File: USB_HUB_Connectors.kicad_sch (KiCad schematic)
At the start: 87 parts, among them IC4 AP22652W6-7, J10 E8124-015-01, J11 E8124-015-01, U15 USB57442G, Y2 ABM8G-25.000MHZ-B4Y-T

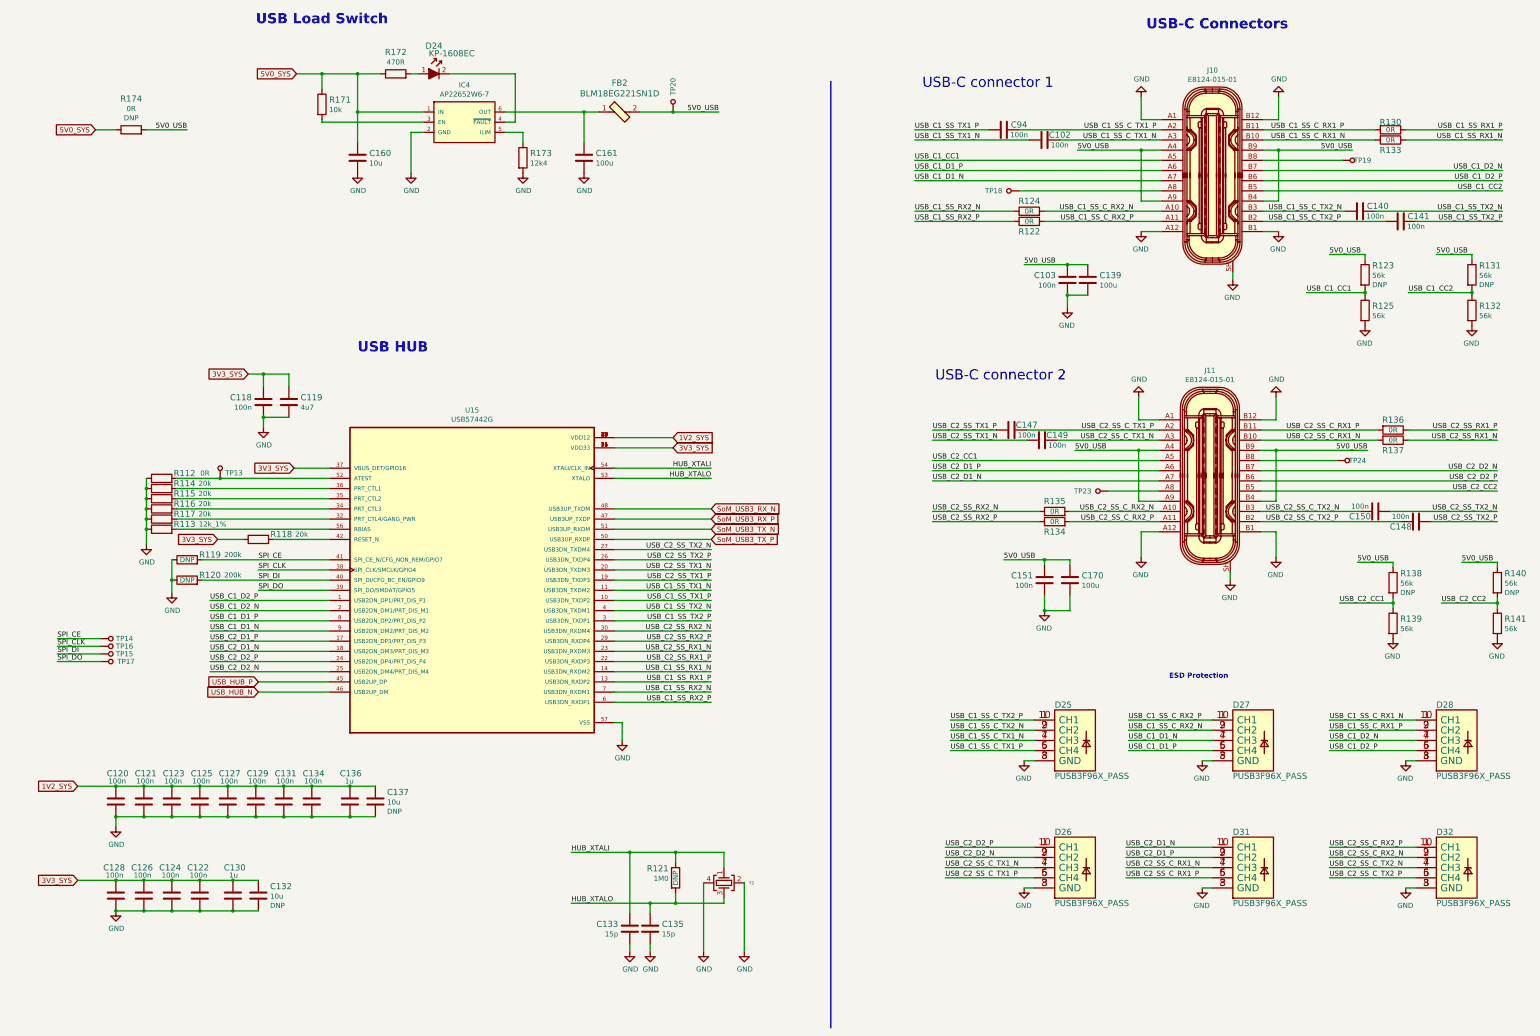
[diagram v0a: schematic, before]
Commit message: Introduce component standardization
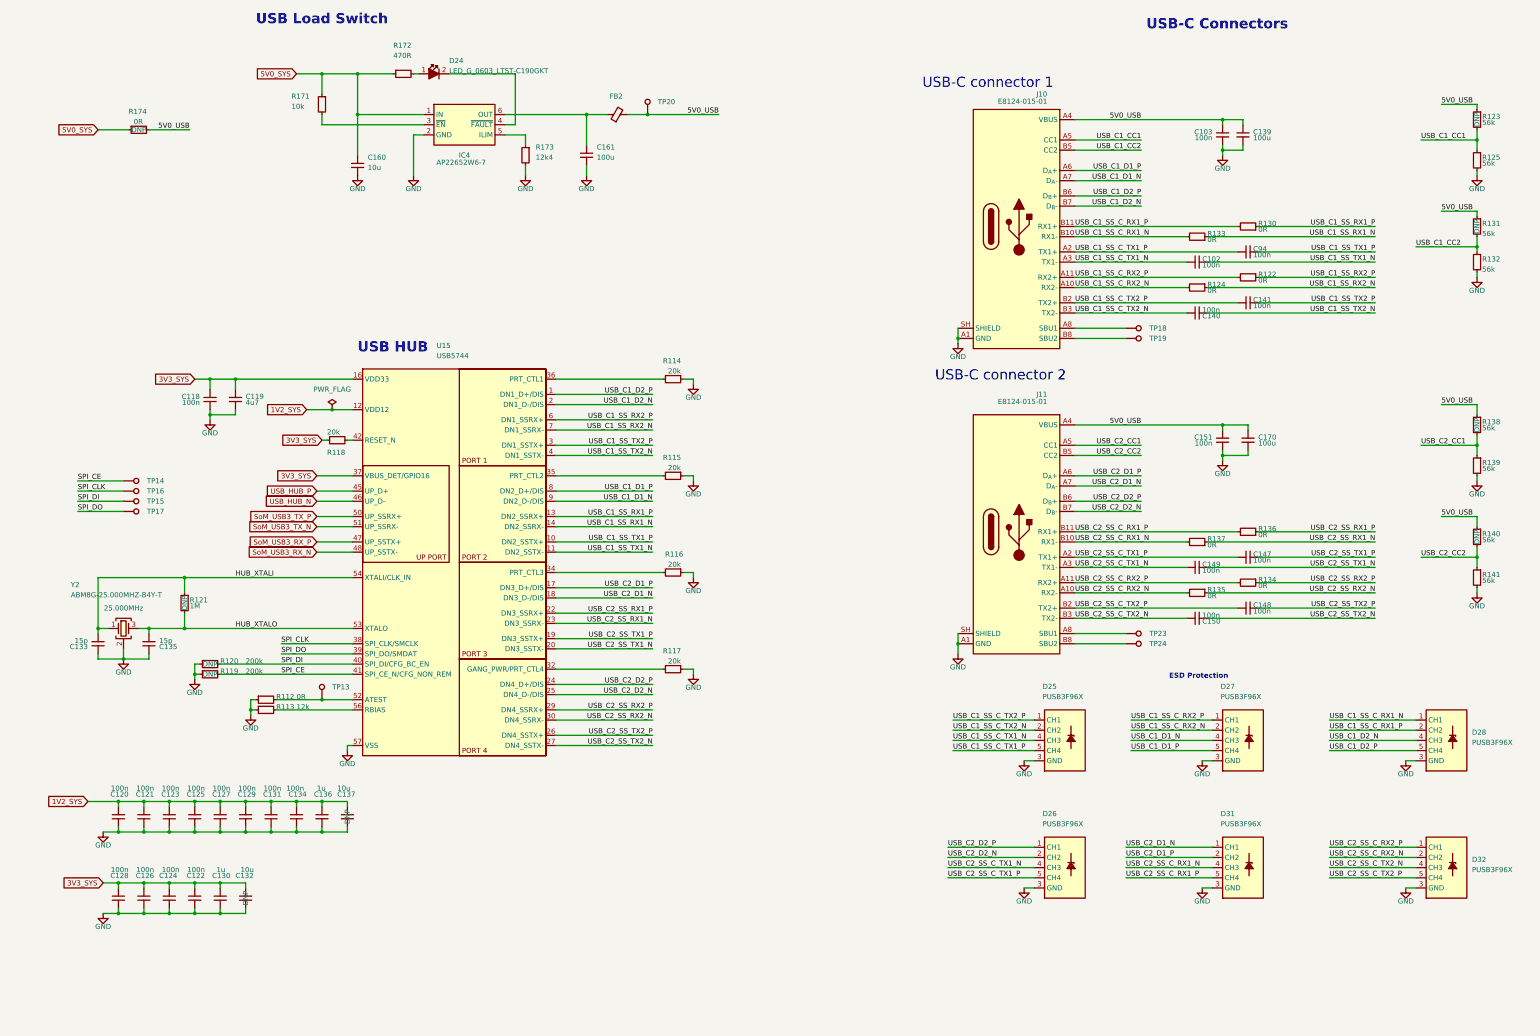
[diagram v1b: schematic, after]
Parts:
- C102, C103, C118, C120, C121, C122, C123, C124, C125, C126, C127, C128, C129, C131, C134, C140, C141, C147, C148, C149, C150, C151, C94: footprint sc606-baseboard-footprints:0402-cap -> sc606-baseboard-footprints:C_0402_1005Metric; Author (none) -> Antmicro; Dielectric (none) -> X5R; License (none) -> Apache-2.0; Voltage (none) -> 50V
- C119: footprint sc606-baseboard-footprints:0402-cap -> sc606-baseboard-footprints:C_0402_1005Metric; Author (none) -> Antmicro; License (none) -> Apache-2.0; Manufacturer MURATA -> Murata
- C130, C136: footprint sc606-baseboard-footprints:0402-cap -> sc606-baseboard-footprints:C_0402_1005Metric; Author (none) -> Antmicro; License (none) -> Apache-2.0
- C132, C137, C160: footprint sc606-baseboard-footprints:0402-cap -> sc606-baseboard-footprints:C_0402_1005Metric; Author (none) -> Antmicro; License (none) -> Apache-2.0; Manufacturer YAGEO -> Yaego
- C133, C135: footprint sc606-baseboard-footprints:0402-cap -> sc606-baseboard-footprints:C_0402_1005Metric; Author (none) -> Antmicro; License (none) -> Apache-2.0; Manufacturer MULTICOMP -> Multicomp
- C139, C161, C170: footprint sc606-baseboard-footprints:0805-cap -> sc606-baseboard-footprints:C_0805_2012Metric; Author (none) -> Antmicro; License (none) -> Apache-2.0; Manufacturer MURATA -> Murata
- D24: value KP-1608EC -> LED_G_0603_LTST-C190GKT; footprint sc606-baseboard-footprints:LED_0603 -> sc606-baseboard-footprints:LED_0603_1608Metric_G; symbol sc606-baseboard:KP-1608EC -> sc606-baseboard:LED_G_0603_LTST-C190GKT; Author (none) -> Antmicro; License (none) -> Apache-2.0; MPN KP-1608EC -> LTST-C190GKT; Manufacturer KINGBRIGHT -> Lite-On Inc.
- D25, D26, D27, D28, D31, D32: footprint sc606-baseboard-footprints:PUSB3F96X -> sc606-baseboard-footprints:Nexperia_DFN-10_2.5x1mm_P0.5mm; Author (none) -> Antmicro; License (none) -> Apache-2.0
- FB2: value BLM18EG221SN1D -> FB_220Z_1A_0603; footprint sc606-baseboard-footprints:0603 -> sc606-baseboard-footprints:FB_0603_1608Metric; symbol sc606-baseboard:BLM18EG221SN1D -> sc606-baseboard:FB_220Z_1A_0603; Author (none) -> Antmicro; License (none) -> Apache-2.0
- IC4: value AP22652W6-7 -> AP22652W6; symbol sc606-baseboard:AP22652W6-7 -> sc606-baseboard:AP22652W6; Author (none) -> Antmicro; License (none) -> Apache-2.0; Manufacturer Diodes Incorporated -> Diodes Incorporated
- J10, J11: value E8124-015-01 -> E8124-015-01_separate; symbol sc606-baseboard:E8124-015-01 -> sc606-baseboard:E8124-015-01_separate; Author (none) -> Antmicro; License (none) -> Apache-2.0; Manufacturer Pulse Electronics Network -> Pulse
- R112, R122, R124, R130, R133, R134, R135, R136, R137, R174: footprint sc606-baseboard-footprints:0402-res -> sc606-baseboard-footprints:R_0402_1005Metric; Author (none) -> Antmicro; Current (none) -> 1A; License (none) -> Apache-2.0; Manufacturer PANASONIC -> Panasonic
- R113: value R_12k_1%_0603 -> R_12k_0603; footprint sc606-baseboard-footprints:0603-res -> sc606-baseboard-footprints:R_0603_1608Metric; symbol sc606-baseboard:R_12k_1%_0603 -> sc606-baseboard:R_12k_0603; Author (none) -> Antmicro; License (none) -> Apache-2.0; MPN MCWR06X1202FTL -> CR0603-FX-1202ELF; Manufacturer MULTICOMP PRO -> Bourns; Tolerance (none) -> 1%; Val 12k_1% -> 12k
- R114, R115, R116, R117, R118: footprint sc606-baseboard-footprints:0402-res -> sc606-baseboard-footprints:R_0402_1005Metric; Author (none) -> Antmicro; License (none) -> Apache-2.0; MPN CRCW040220K0FKED -> CR0402-FX-2002GLF; Manufacturer VISHAY -> Bourns; Tolerance (none) -> 1%
- R119, R120: footprint sc606-baseboard-footprints:0402-res -> sc606-baseboard-footprints:R_0402_1005Metric; Author (none) -> Antmicro; License (none) -> Apache-2.0; MPN RC0402FR-07200KL -> CR0402-FX-2003GLF; Manufacturer YAGEO_(PHYCOMP) -> Bourns; Tolerance (none) -> 1%
- R121: value R_1M0_0402 -> R_1M_0402; footprint sc606-baseboard-footprints:0402-res -> sc606-baseboard-footprints:R_0402_1005Metric; symbol sc606-baseboard:R_1M0_0402 -> sc606-baseboard:R_1M_0402; Author (none) -> Antmicro; License (none) -> Apache-2.0; MPN CRG0402F1M0 -> CR0402-FX-1004GLF; Manufacturer TE CONNECTIVITY -> Bourns; Tolerance (none) -> 1%; Val 1M0 -> 1M
- R123, R125, R131, R132, R138, R139, R140, R141: footprint sc606-baseboard-footprints:0402-res -> sc606-baseboard-footprints:R_0402_1005Metric; Author (none) -> Antmicro; License (none) -> Apache-2.0; MPN CRCW040256K0FKED -> CR0402-FX-5602GLF; Manufacturer VISHAY -> Bourns; Tolerance (none) -> 1%
- R171: footprint sc606-baseboard-footprints:0402-res -> sc606-baseboard-footprints:R_0402_1005Metric; Author (none) -> Antmicro; License (none) -> Apache-2.0; MPN CRCW040210K0FKEDHP -> CR0402-FX-1002GLF; Manufacturer VISHAY -> Bourns; Tolerance (none) -> 1%
- R172: footprint sc606-baseboard-footprints:0402-res -> sc606-baseboard-footprints:R_0402_1005Metric; Author (none) -> Antmicro; License (none) -> Apache-2.0; MPN CRCW0402470RFKED -> CR0402-FX-4700GLF; Manufacturer VISHAY -> Bourns; Tolerance (none) -> 1%
- R173: footprint sc606-baseboard-footprints:0402-res -> sc606-baseboard-footprints:R_0402_1005Metric; Author (none) -> Antmicro; License (none) -> Apache-2.0; MPN ERJ2RKF1242X -> CR0402-FX-1242GLF; Manufacturer PANASONIC_ELECTRONIC_COMPONENTS -> Bourns; Tolerance (none) -> 1%
- TP13, TP14, TP15, TP16, TP17: value TP_SMD_1_5MM -> TP_1.5mm_SMD; footprint sc606-baseboard-footprints:TP-R-1.5 -> sc606-baseboard-footprints:TP_SMD_1.5mm; symbol sc606-baseboard:TP_SMD_0_75MM-antmicroTestPoints -> sc606-baseboard:TP_1.5mm_SMD; Author (none) -> Antmicro; License (none) -> Apache-2.0
- TP18, TP19, TP20, TP23, TP24: value TP_SMD_1_5MM -> TP_1.5mm_SMD; footprint sc606-baseboard-footprints:TP-R-1.5 -> sc606-baseboard-footprints:TP_SMD_1.5mm; symbol sc606-baseboard:TP_SMD_0_75MM -> sc606-baseboard:TP_1.5mm_SMD; Author (none) -> Antmicro; License (none) -> Apache-2.0
- U15: footprint sc606-baseboard-footprints:QFN40P700X700X100-57N -> sc606-baseboard-footprints:QFN-56-1EP_7x7mm_P0.4mm_EP4.6x4.6mm; Author (none) -> Antmicro; License (none) -> Apache-2.0; Manufacturer MICROCHIP -> Microchip
- Y2: footprint sc606-baseboard-footprints:KX-7 -> sc606-baseboard-footprints:Oscillator_SMD_Geyer_KX-7-4Pin_3.2x2.5mm; Author (none) -> Antmicro; License (none) -> Apache-2.0; Val (none) -> 25.000MHz
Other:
- moved on the sheet: C102, C103, C118, C119, C120, C121, C122, C123, C124, C125, C126, C127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

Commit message: [#61796] Run globlib
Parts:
- C102, C103, C118, C120, C121, C122, C123, C124, C125, C126, C127, C128, C129, C131, C134, C140, C141, C147, C148, C149, C150, C151, C94: footprint sc606-baseboard-footprints:C_0402_1005Metric -> antmicro-footprints:C_0402_1005Metric; symbol sc606-baseboard:C_100n_0402 -> antmicroCapacitors0402:C_100n_0402
- C119: footprint sc606-baseboard-footprints:C_0402_1005Metric -> antmicro-footprints:C_0402_1005Metric; symbol sc606-baseboard:C_4u7_0402 -> antmicroCapacitors0402:C_4u7_0402
- C130, C136: footprint sc606-baseboard-footprints:C_0402_1005Metric -> antmicro-footprints:C_0402_1005Metric; symbol sc606-baseboard:C_1u_0402 -> antmicroCapacitors0402:C_1u_0402
- C132, C137, C160: footprint sc606-baseboard-footprints:C_0402_1005Metric -> antmicro-footprints:C_0402_1005Metric; symbol sc606-baseboard:C_10u_0402 -> antmicroCapacitors0402:C_10u_0402
- C133, C135: footprint sc606-baseboard-footprints:C_0402_1005Metric -> antmicro-footprints:C_0402_1005Metric; symbol sc606-baseboard:C_15p_0402 -> antmicroCapacitors0402:C_15p_0402
- C139, C161, C170: footprint sc606-baseboard-footprints:C_0805_2012Metric -> antmicro-footprints:C_0805_2012Metric; symbol sc606-baseboard:C_100u_0805 -> antmicroCapacitorsmisc:C_100u_0805
- D24: footprint sc606-baseboard-footprints:LED_0603_1608Metric_G -> antmicro-footprints:LED_0603_1608Metric_G; symbol sc606-baseboard:LED_G_0603_LTST-C190GKT -> antmicroLEDIndicationDiscrete:LED_G_0603_LTST-C190GKT
- D25, D26, D27, D28, D31, D32: footprint sc606-baseboard-footprints:Nexperia_DFN-10_2.5x1mm_P0.5mm -> antmicro-footprints:Nexperia_DFN-10_2.5x1mm_P0.5mm; symbol sc606-baseboard:PUSB3F96X_PASS -> antmicroTVSDiodes:PUSB3F96X_PASS
- FB2: footprint sc606-baseboard-footprints:FB_0603_1608Metric -> antmicro-footprints:FB_0603_1608Metric; symbol sc606-baseboard:FB_220Z_1A_0603 -> antmicroFerriteBeadsandChips:FB_220Z_1A_Murata-BLM18EG_0603
- IC4: footprint sc606-baseboard-footprints:SOT-23-6 -> antmicro-footprints:SOT-23-6; symbol sc606-baseboard:AP22652W6 -> antmicroPMICPowerDistributionSwitchesLoadDrivers:AP22652W6
- J10, J11: footprint sc606-baseboard-footprints:USB-C_Female_E8124-015-01 -> antmicro-footprints:USB-C_Receptacle_PulseElectronics_E8124-015-01; symbol sc606-baseboard:E8124-015-01_separate -> antmicroUSBConnectors:USB-C_PulseElectronics_E8124-015-01
- R112, R122, R124, R130, R133, R134, R135, R136, R137, R174: footprint sc606-baseboard-footprints:R_0402_1005Metric -> antmicro-footprints:R_0402_1005Metric; symbol sc606-baseboard:R_0R_0402 -> antmicroResistors0402:R_0R_0402
- R113: footprint sc606-baseboard-footprints:R_0603_1608Metric -> antmicro-footprints:R_0603_1608Metric; symbol sc606-baseboard:R_12k_0603 -> antmicroResistors0603:R_12k_0603
- R114, R115, R116, R117, R118: footprint sc606-baseboard-footprints:R_0402_1005Metric -> antmicro-footprints:R_0402_1005Metric; symbol sc606-baseboard:R_20k_0402 -> antmicroResistors0402:R_20k_0402
- R119, R120: footprint sc606-baseboard-footprints:R_0402_1005Metric -> antmicro-footprints:R_0402_1005Metric; symbol sc606-baseboard:R_200k_0402 -> antmicroResistors0402:R_200k_0402
- R121: footprint sc606-baseboard-footprints:R_0402_1005Metric -> antmicro-footprints:R_0402_1005Metric; symbol sc606-baseboard:R_1M_0402 -> antmicroResistors0402:R_1M_0402
- R123, R125, R131, R132, R138, R139, R140, R141: footprint sc606-baseboard-footprints:R_0402_1005Metric -> antmicro-footprints:R_0402_1005Metric; symbol sc606-baseboard:R_56k_0402 -> antmicroResistors0402:R_56k_0402
- R171: footprint sc606-baseboard-footprints:R_0402_1005Metric -> antmicro-footprints:R_0402_1005Metric; symbol sc606-baseboard:R_10k_0402 -> antmicroResistors0402:R_10k_0402
- R172: footprint sc606-baseboard-footprints:R_0402_1005Metric -> antmicro-footprints:R_0402_1005Metric; symbol sc606-baseboard:R_470R_0402 -> antmicroResistors0402:R_470R_0402
- R173: footprint sc606-baseboard-footprints:R_0402_1005Metric -> antmicro-footprints:R_0402_1005Metric; symbol sc606-baseboard:R_12k4_0402 -> antmicroResistors0402:R_12k4_0402
- TP13, TP14, TP15, TP16, TP17, TP18, TP19, TP20, TP23, TP24: footprint sc606-baseboard-footprints:TP_SMD_1.5mm -> antmicro-footprints:TP_SMD_1.5mm; symbol sc606-baseboard:TP_1.5mm_SMD -> antmicroTestPoints:TP_1.5mm_SMD
- U15: footprint sc606-baseboard-footprints:QFN-56-1EP_7x7mm_P0.4mm_EP4.6x4.6mm -> antmicro-footprints:QFN-56-1EP_7x7mm_P0.4mm_EP4.6x4.6mm; symbol sc606-baseboard:USB57442G -> antmicroInterfaceControllers:USB57442G

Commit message: [#61796] Update schematics
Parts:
- C132, C137: Manufacturer Yaego -> YAGEO; now not fitted; now left out of the parts list
- C133, C135: MPN MC0402N150J500CT -> C0402C150K5GACTU.; Manufacturer Multicomp -> KEMET
- C160: Manufacturer Yaego -> YAGEO
- D24: Color (none) -> Green; Manufacturer Lite-On Inc. -> Lite-On
- FB2: value FB_220Z_1A_0603 -> FB_220Z_1A_Murata-BLM18EG_0603; Val (none) -> 220Z/1A
- J10, J11: value E8124-015-01_separate -> USB-C_PulseElectronics_E8124-015-01; Manufacturer Pulse -> Pulse Electronics
- R119, R120, R121, R123, R131, R138, R140, R174: now not fitted; now left out of the parts list
- U15: MPN USB5744 -> USB5744/2G; Manufacturer Microchip -> Microchip Technology
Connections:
- net at IC4.4 (~{FAULT}): now also D24.1 (C); no longer D24.2
- net at R172.2: now also D24.2 (A); no longer D24.1
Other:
- company: (none) -> Antmicro Ltd
- moved on the sheet: C120, C128, C140, C141, C148, C150, C160, D24, D25, D26, D27, D28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

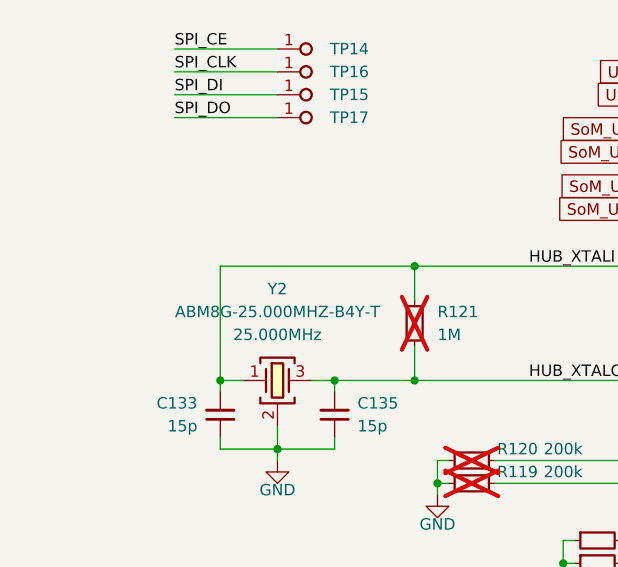
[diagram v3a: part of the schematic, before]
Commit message: [#61796] Clean ERC
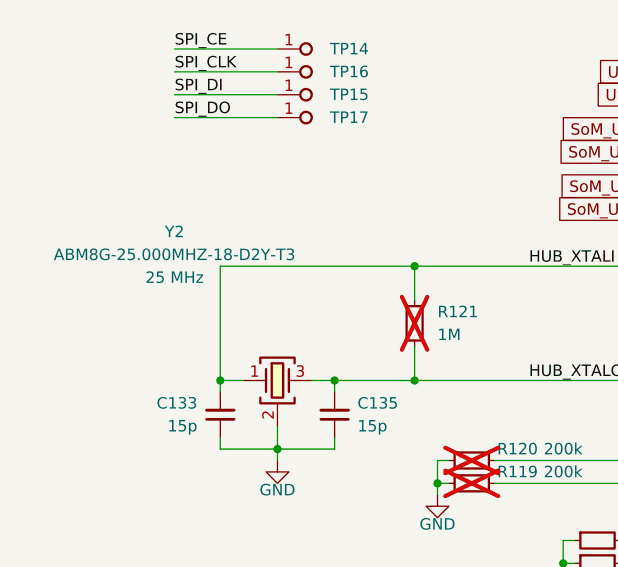
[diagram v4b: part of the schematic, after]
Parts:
- Y2: value ABM8G-25.000MHZ-B4Y-T -> Resonator_25MHz_ABM8G; footprint sc606-baseboard-footprints:Oscillator_SMD_Geyer_KX-7-4Pin_3.2x2.5mm -> antmicro-footprints:Resonator_SMD_Abracon_ABM8G_3.2x2.5mm; symbol sc606-baseboard:ABM8G-25.000MHZ-B4Y-T -> antmicroResonators:Resonator_25MHz_ABM8G; MPN ABM8G-25.000MHZ-B4Y-T -> ABM8G-25.000MHZ-18-D2Y-T3; Val 25.000MHz -> 25 MHz
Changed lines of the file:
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@@
     )
   )
-  (symbol (lib_id "sc606-baseboard:ABM8G-25.000MHZ-B4Y-T") (at 39.37 176.53 0) (unit 1)
-    (in_bom yes) (on_board yes) (dnp no) (fields_autoplaced)
-    (property "Reference" "Y2" (at 43.18 166.37 0)
+  (symbol (lib_id "antmicroResonators:Resonator_25MHz_ABM8G") (at 39.37 176.53 0) (unit 1)
+    (in_bom yes) (on_board yes) (dnp no)
+    (property "Reference" "Y2" (at 31.75 160.02 0)
       (effects (font (size 1.27 1.27) (thickness 0.15)))
     )
-    (property "Value" "ABM8G-25.000MHZ-B4Y-T" (at 43.18 168.91 0)
+    (property "Value" "Resonator_25MHz_ABM8G" (at 54.61 189.23 0)
+      (effects (font (size 1.27 1.27) (thickness 0.15)) (justify left bottom) hide)
+    )
+    (property "Footprint" "antmicro-footprints:Resonator_SMD_Abracon_ABM8G_3.2x2.5mm" (at 54.61 191.77 0)
+      (effects (font (size 1.27 1.27) (thickness 0.15)) (justify left bottom) hide)
+    )
+    (property "Datasheet" "https://abracon.com/Resonators/ABM8G.pdf" (at 54.61 194.31 0)
+      (effects (font (size 1.27 1.27) (thickness 0.15)) (justify left bottom) hide)
+    )
+    (property "MPN" "ABM8G-25.000MHZ-18-D2Y-T3" (at 31.75 162.56 0)
       (effects (font (size 1.27 1.27) (thickness 0.15)))
     )
-    (property "Footprint" "sc606-baseboard-footprints:Oscillator_SMD_Geyer_KX-7-4Pin_3.2x2.5mm" (at 62.23 186.69 0)
+    (property "Manufacturer" "Abracon" (at 54.61 196.85 0)
       (effects (font (size 1.27 1.27) (thickness 0.15)) (justify left bottom) hide)
     )
-    (property "Datasheet" "" (at 62.23 189.23 0)
+    (property "Author" "Antmicro" (at 54.61 199.39 0)
       (effects (font (size 1.27 1.27) (thickness 0.15)) (justify left bottom) hide)
     )
-    (property "MPN" "ABM8G-25.000MHZ-B4Y-T" (at 62.23 191.77 0)
+    (property "License" "Apache-2.0" (at 54.61 201.93 0)
       (effects (font (size 1.27 1.27) (thickness 0.15)) (justify left bottom) hide)
     )
-    (property "Manufacturer" "Abracon" (at 62.23 194.31 0)
-      (effects (font (size 1.27 1.27) (thickness 0.15)) (justify left bottom) hide)
-    )
-    (property "Author" "Antmicro" (at 62.23 196.85 0)
-      (effects (font (size 1.27 1.27) (thickness 0.15)) (justify left bottom) hide)
-    )
-    (property "License" "Apache-2.0" (at 62.23 199.39 0)
-      (effects (font (size 1.27 1.27) (thickness 0.15)) (justify left bottom) hide)
-    )
-    (property "Val" "25.000MHz" (at 43.18 171.45 0)
-      (effects (font (size 1.27 1.27)))
+    (property "Val" "25 MHz" (at 31.75 165.1 0)
+      (effects (font (size 1.27 1.27) (thickness 0.15)))
     )
     (pin "1")
